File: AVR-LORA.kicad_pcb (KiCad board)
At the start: 2 copper layers, 51.4 x 29.2 mm, 36 parts, among them J1 Batt, J2 Solar, J3 SMA, J4 CONN_01X14, J5 CONN_01X14, U1 MCP1700-3302E_SOT23, U2 RFM95HW, U3 AVR128DB28, Y1 24MHz, Y2 32768Hz

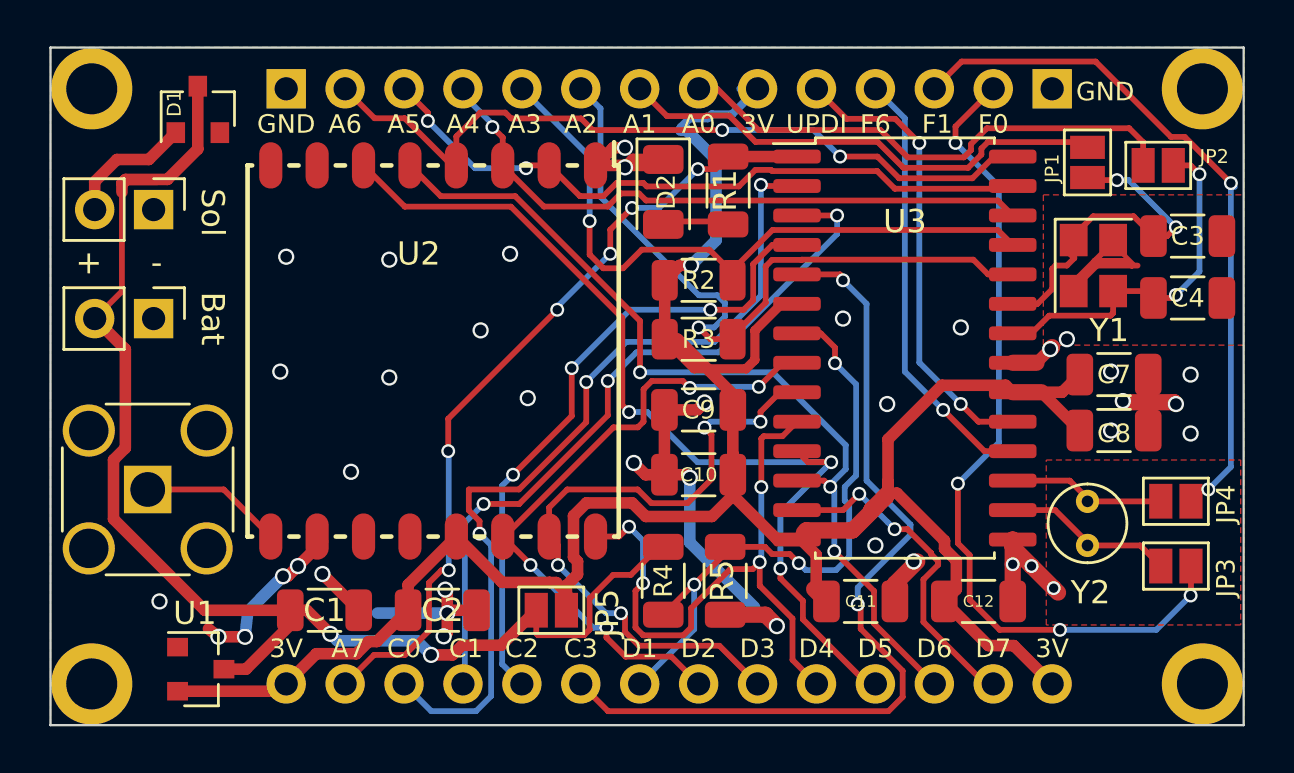
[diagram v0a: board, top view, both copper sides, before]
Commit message: Bigger SMA central pad for soldering wire
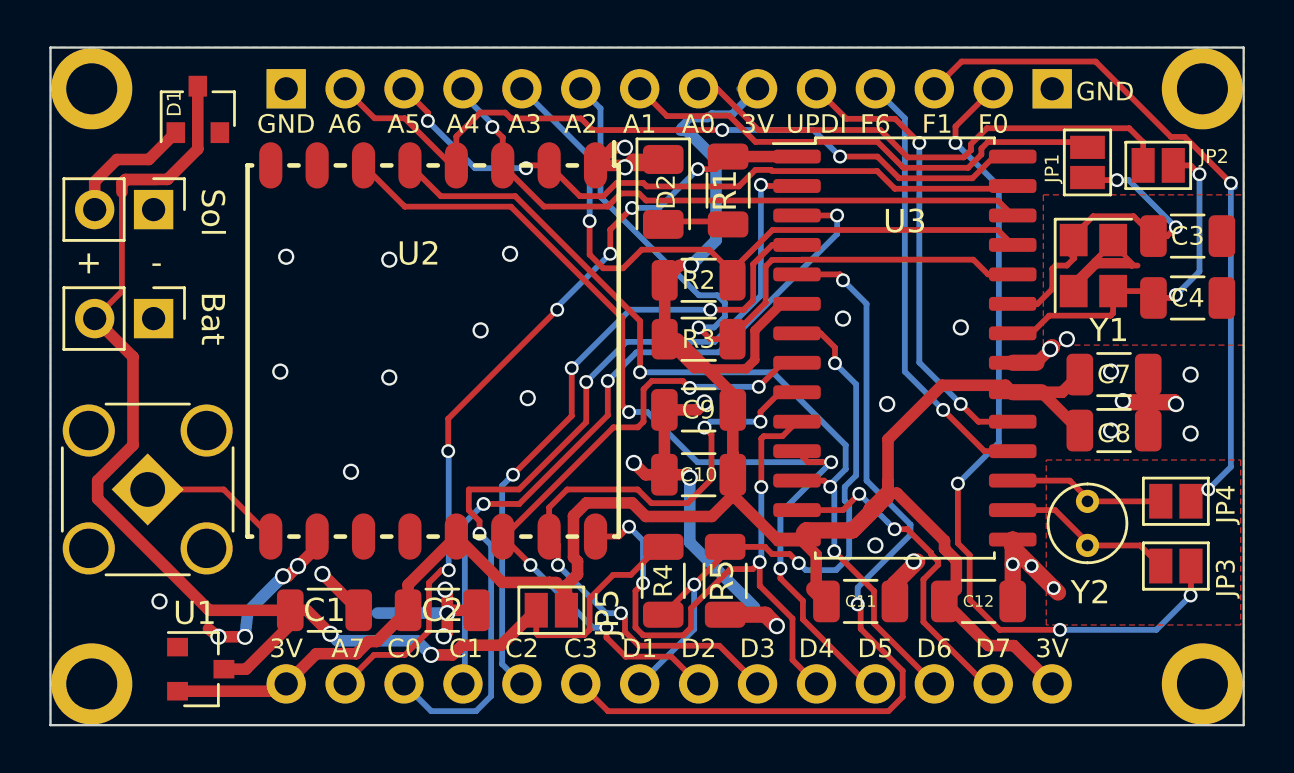
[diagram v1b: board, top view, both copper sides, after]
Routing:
- net VCC: track 59.1 -> 59.8 mm
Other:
- rule pad_to_mask_clearance: 0.1 -> 0

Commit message: Grow board slightly
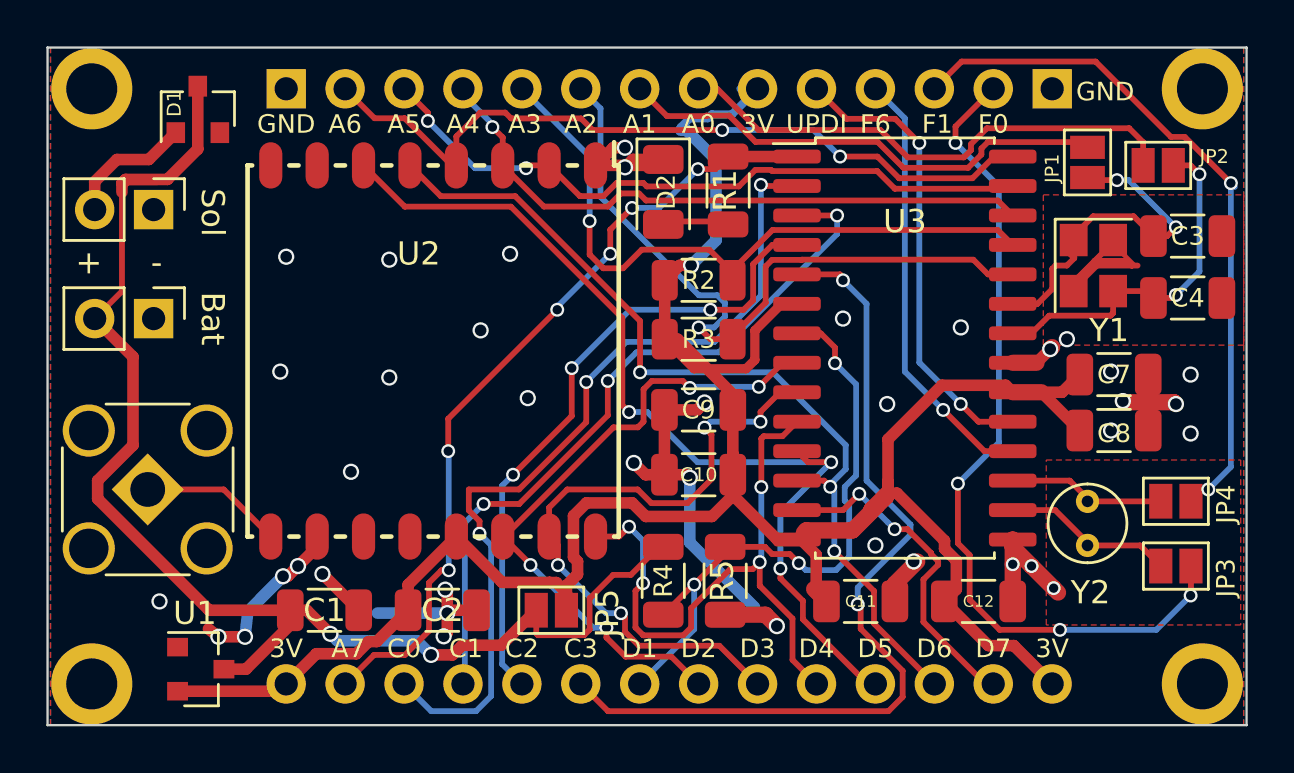
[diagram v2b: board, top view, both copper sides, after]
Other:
- board size 51.4 x 29.2 mm -> 51.7 x 29.2 mm

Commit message: Improve ground plane
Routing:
- net /A2: track 30.6 -> 28.9 mm, vias 1 -> 3
- net /A3: track 29.5 -> 30.9 mm
- net /C2: track 28.0 -> 29.1 mm
- net /A7: track 34.7 -> 35.7 mm
- net /C1: track 31.9 -> 32.8 mm
- net GND: track 67.8 -> 66.9 mm
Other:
- board text added: "AVRxDB28 v1.0 v7f.eu"
- board text added: "RFM95"

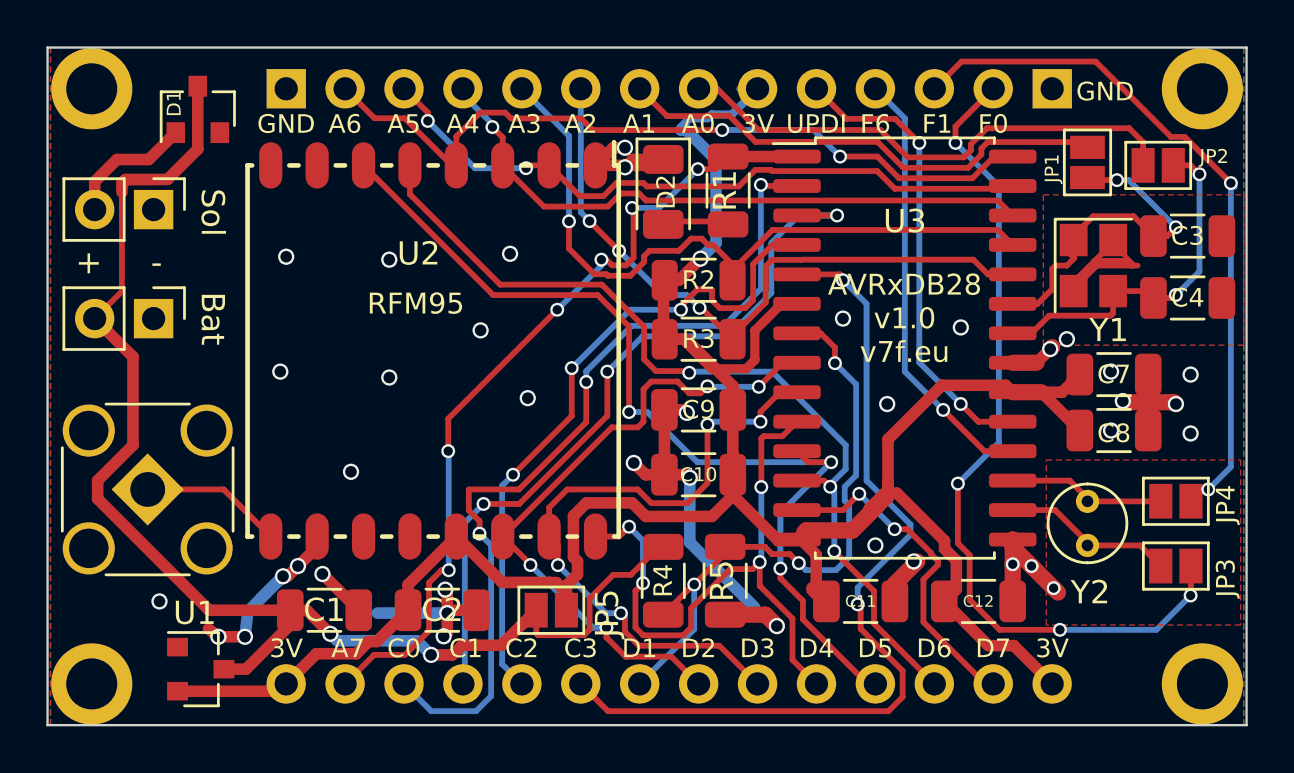
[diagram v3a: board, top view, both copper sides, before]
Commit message: Improve silk screen
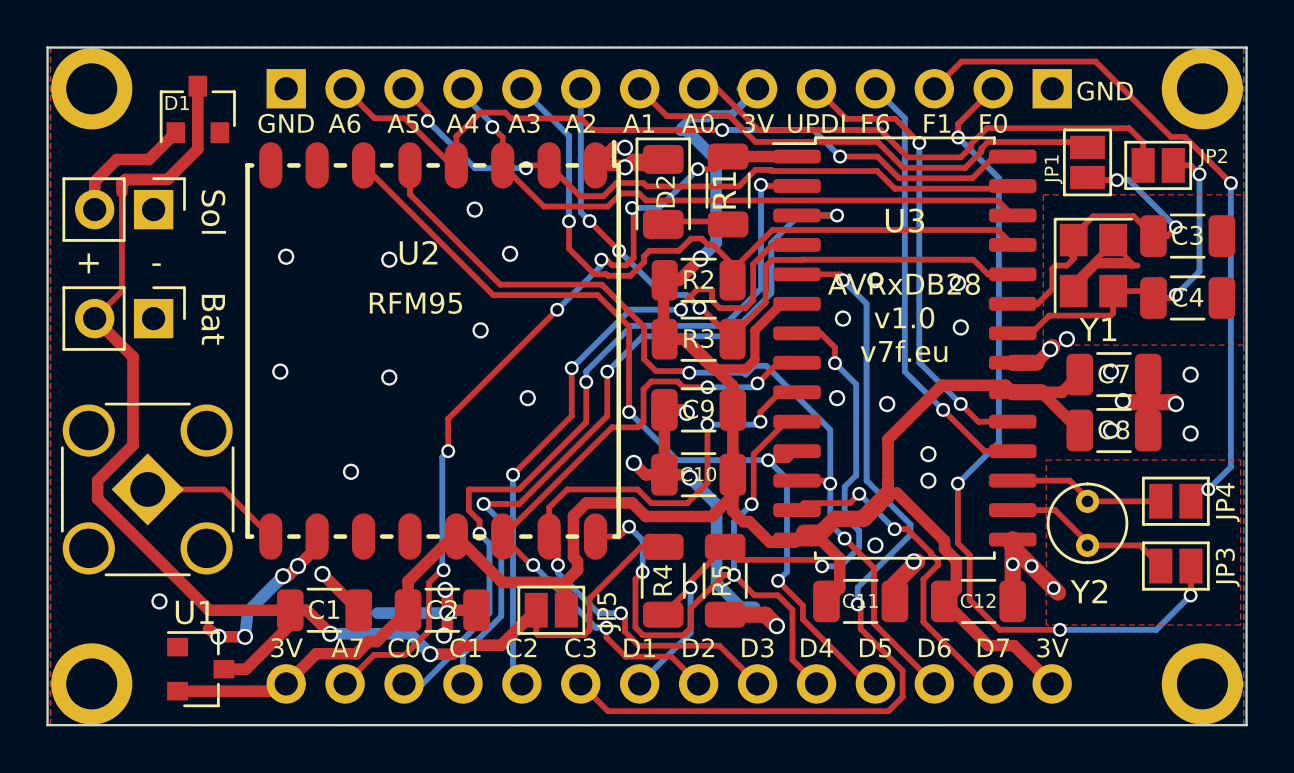
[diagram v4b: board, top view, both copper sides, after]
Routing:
- net /D5: track 41.6 -> 38.3 mm
- net /C0: track 37.3 -> 34.3 mm
- net /3V3: track 113.2 -> 114.6 mm
- net /C1: track 32.8 -> 33.5 mm
- net GND: track 66.9 -> 67.2 mm, vias 39 -> 45

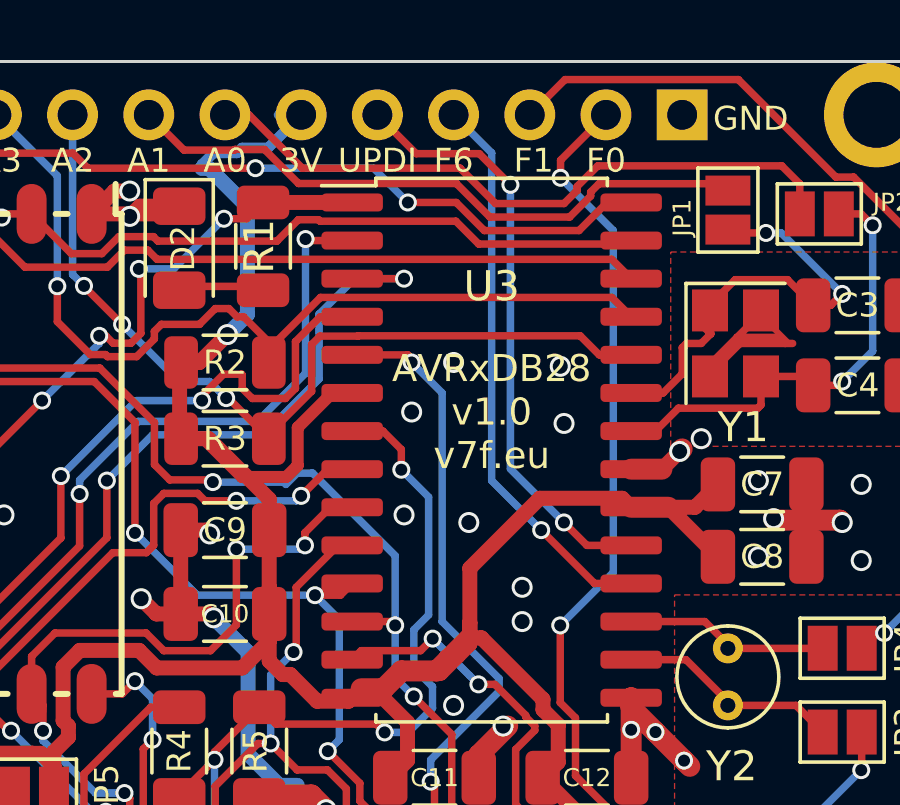
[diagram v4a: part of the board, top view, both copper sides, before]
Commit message: Improve ground plane
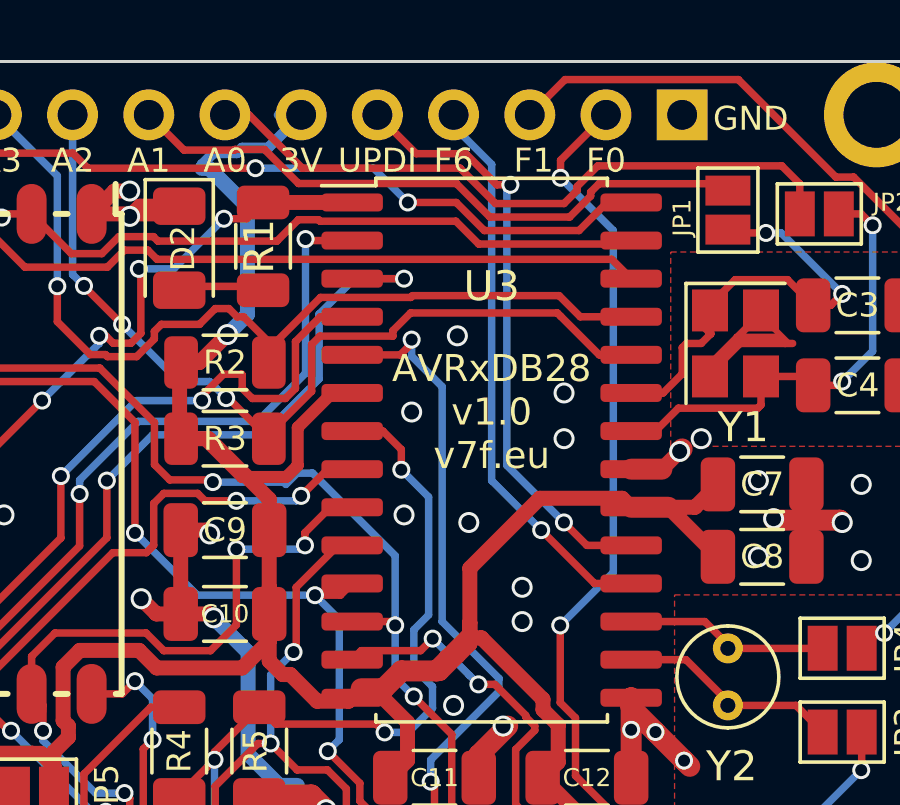
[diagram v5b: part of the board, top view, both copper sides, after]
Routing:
- net /A2: track 28.9 -> 29.6 mm
- net /C3: track 37.7 -> 38.3 mm

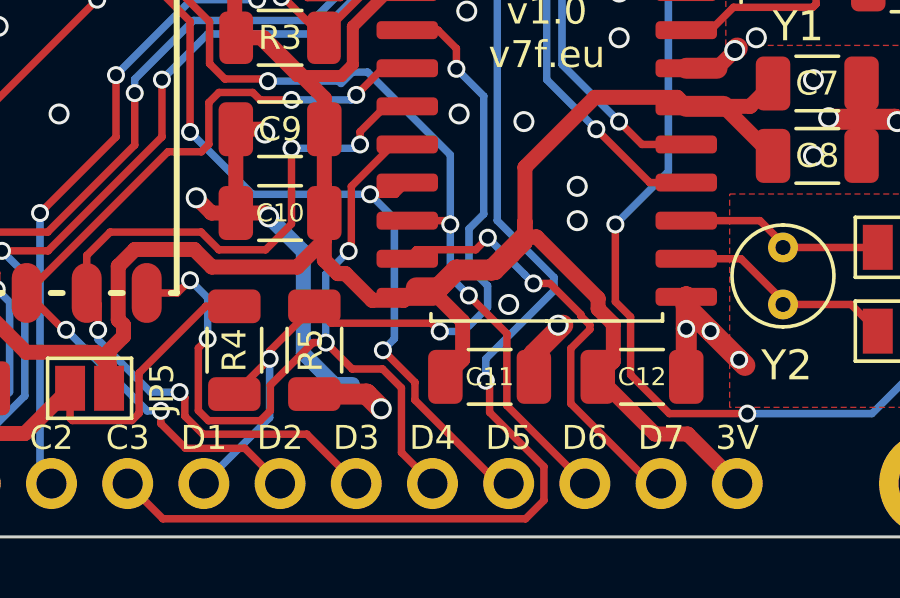
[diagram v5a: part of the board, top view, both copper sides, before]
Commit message: Improve ground plane
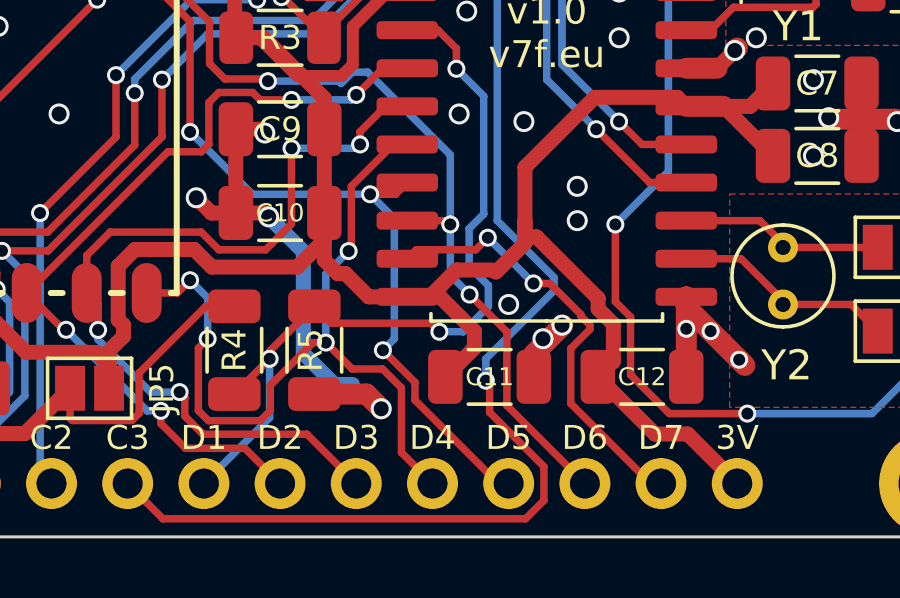
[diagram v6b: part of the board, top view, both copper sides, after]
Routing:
- net /3V3: track 114.6 -> 110.1 mm
- net GND: vias 45 -> 46
